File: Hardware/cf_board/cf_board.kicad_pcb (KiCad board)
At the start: 2 copper layers, 80.8 x 60.1 mm, 19 parts, among them J1 Conn_01x40, J2 Conn_02x25_Top_Bottom, U1 74HC00, U2 74HC00

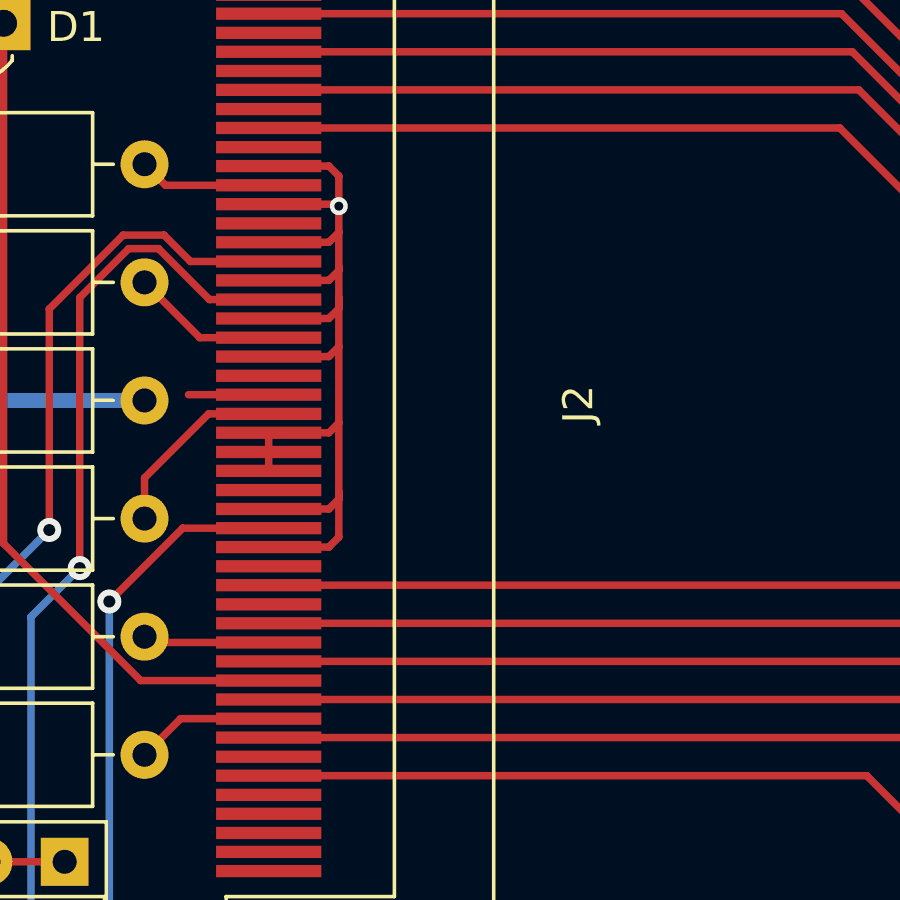
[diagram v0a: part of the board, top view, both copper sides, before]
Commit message: add jlc reference
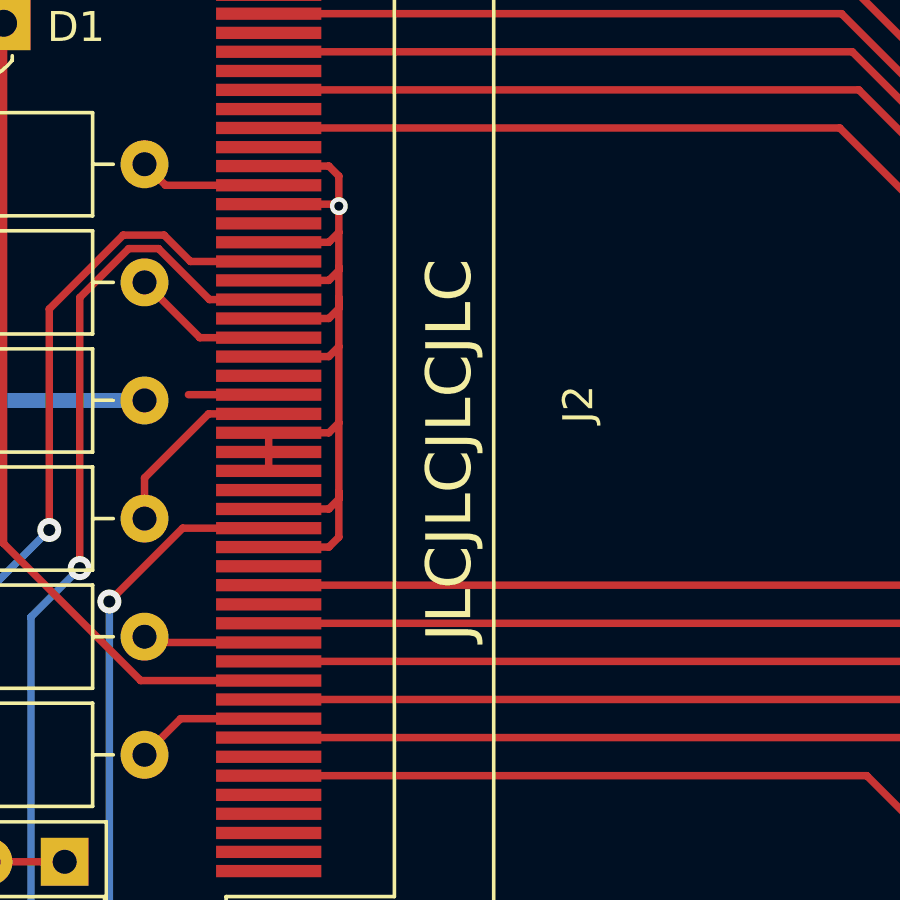
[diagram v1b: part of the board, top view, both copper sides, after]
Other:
- board text added: "JLCJLCJLCJLC"
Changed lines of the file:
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@@
     (effects (font (size 0.8 0.8) (thickness 0.15)))
+  )
+  (gr_text "JLCJLCJLCJLC" (at 120.65 86.614 90) (layer "F.SilkS")
+    (effects (font (size 1.5 1.5) (thickness 0.3)))
   )
   (gr_text "Compact Flash Board ${VERSION}" (at 81.407 68.707) (layer "F.SilkS")

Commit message: update with lcsc CF card socket
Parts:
- removed J2: Conn_02x25_Top_Bottom, Connector_Card:CF-Card_3M_N7E50-A516xx-30
- added J3: Conn_02x26_Top_Bottom, Custom_Footprints:SD-SMD_CFH-L3C1LBL01MN0, F.Cu at (121.7, 85.6)
- moved R2 19.7 mm to (110.5, 96.8)
- moved R3 19.7 mm to (110.5, 77.1)
- moved R1 11.8 mm to (110.5, 81.0)
- moved R4 11.8 mm to (110.5, 92.8)
- moved R5 3.94 mm to (110.5, 85.0)
- moved R6 3.94 mm to (97.8, 88.9)
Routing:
- net D3: track 69.6 -> 40.4 mm, vias 1 -> 0
- net D4: track 67.3 -> 38.9 mm
- net D5: track 65.2 -> 39.2 mm
- net D6: track 63.0 -> 38.5 mm
- net D7: track 60.3 -> 37.3 mm
- net D2: track 45.9 -> 68.3 mm, vias 0 -> 1
- net D1: track 49.0 -> 70.4 mm, vias 0 -> 1
- net D0: track 52.1 -> 72.5 mm, vias 0 -> 1
- net A0: track 50.6 -> 69.5 mm, vias 0 -> 1
- net A1: track 51.0 -> 65.8 mm
- net Net-(D1-Pad1): track 28.1 -> 14.9 mm
- net ~{RESET}: track 40.2 -> 49.6 mm
- net Net-(U2-Pad8): track 46.1 -> 36.9 mm
- net A2: track 51.8 -> 60.6 mm
- net Net-(U2-Pad11): track 39.1 -> 30.9 mm
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
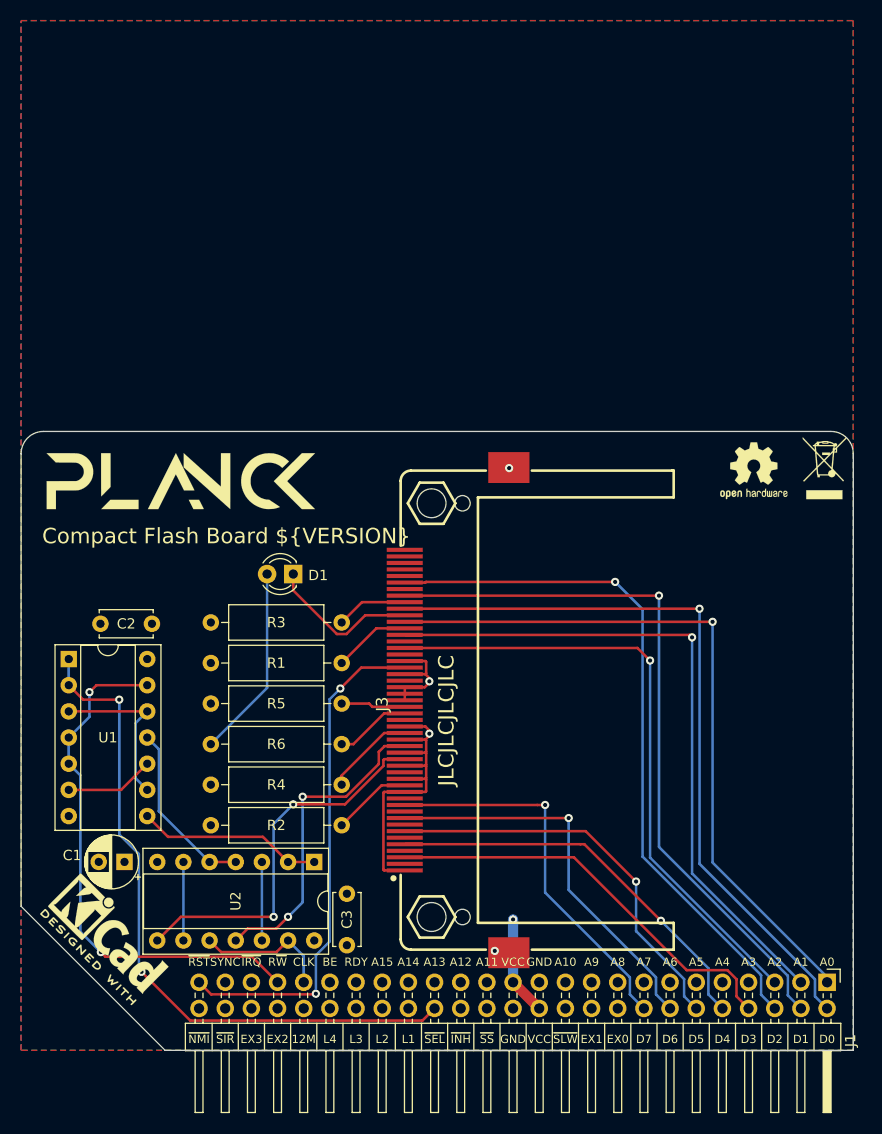
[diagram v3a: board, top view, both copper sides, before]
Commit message: CF card works as block storage for forth
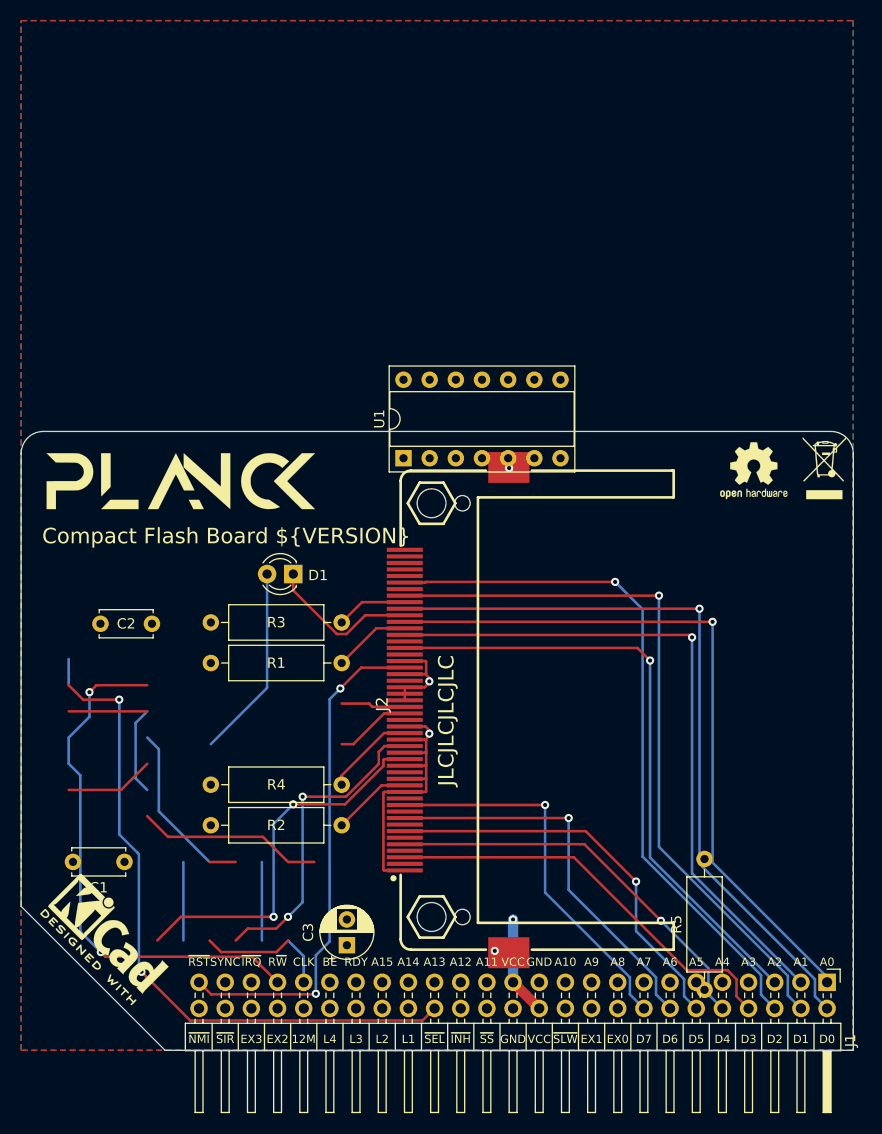
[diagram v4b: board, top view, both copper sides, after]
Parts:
- removed J3: Conn_02x26_Top_Bottom, Custom_Footprints:SD-SMD_CFH-L3C1LBL01MN0
- removed R6: 500R, Resistor_THT:R_Axial_DIN0309_L9.0mm_D3.2mm_P12.70mm_Horizontal
- removed U2: 74HC00, Package_DIP:DIP-14_W7.62mm_Socket
- added J2: Conn_02x26_Top_Bottom, Custom_Footprints:SD-SMD_CFH-L3C1LBL01MN0, F.Cu at (121.7, 85.6)
- C1: value 10u -> 100n; footprint Capacitor_THT:CP_Radial_D5.0mm_P2.50mm -> Capacitor_THT:C_Disc_D5.0mm_W2.5mm_P5.00mm
- C3: value 100n -> 10u; footprint Capacitor_THT:C_Disc_D5.0mm_W2.5mm_P5.00mm -> Capacitor_THT:CP_Radial_D5.0mm_P2.50mm
- R5: value 1k -> 500R
- moved R5 44.9 mm to (145.7, 112.7), turned to 90 degrees
- moved U1 37.9 mm to (116.5, 61.1), turned to 90 degrees
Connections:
- R5 pad 1: Net-(R5-Pad1) -> Net-(D1-Pad2)
- U1 pad 1: ~{SLOT_SEL} -> (no net)
- U1 pad 10: Net-(U1-Pad10) -> CLK
- U1 pad 13: R~{W} -> CLK
- U1 pad 2: ~{SLOT_SEL} -> (no net)
- U1 pad 3: Net-(U1-Pad12) -> (no net)
- U1 pad 6: Net-(U1-Pad10) -> Net-(U1-Pad12)
- U1 pad 9: Net-(U1-Pad12) -> R~{W}
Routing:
- net (no net): track 0.00 -> 58.1 mm
- net GND: track 40.8 -> 92.4 mm, vias 4 -> 5
- net Net-(U2-Pad8): track 36.9 -> 0.00 mm, vias 2 -> 0
- net R~{W}: track 51.6 -> 17.1 mm, vias 2 -> 1
- net Net-(U2-Pad11): track 30.9 -> 0.00 mm, vias 2 -> 0
- net Net-(J2-Pad34): track 18.1 -> 36.9 mm, vias 0 -> 2
- net Net-(U1-Pad12): track 16.2 -> 0.00 mm
- net Net-(J2-Pad35): track 17.1 -> 30.9 mm, vias 0 -> 2
- net Net-(U1-Pad10): track 8.67 -> 0.00 mm
- net Net-(U2-Pad6): track 7.62 -> 0.00 mm
- net Net-(U2-Pad12): track 7.62 -> 0.00 mm
- net +5V: track 17.1 -> 23.3 mm
- net Net-(R5-Pad1): track 6.26 -> 0.00 mm

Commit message: Add clock stretching + Simplify decoding.
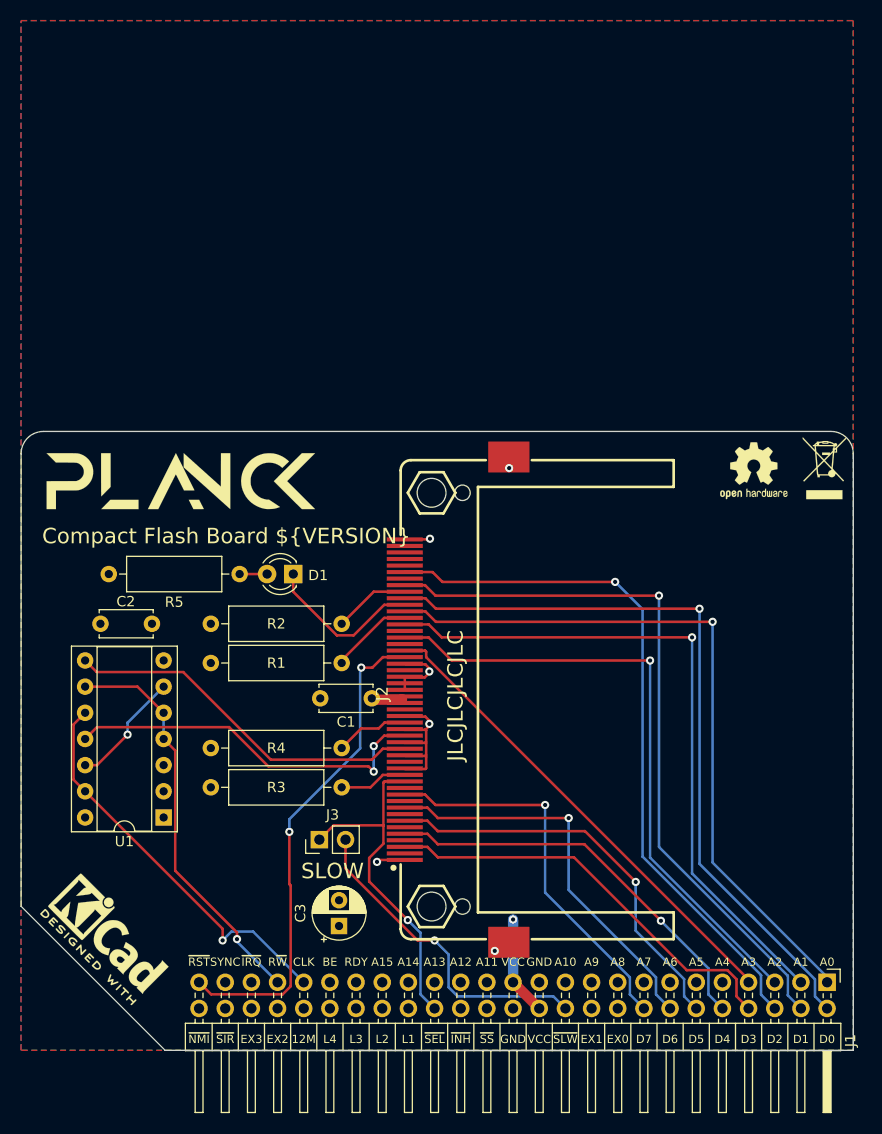
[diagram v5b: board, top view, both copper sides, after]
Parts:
- added J3: Conn_01x02, Connector_PinHeader_2.54mm:PinHeader_1x02_P2.54mm_Vertical, F.Cu at (108.3, 98.2)
- moved R5 60.5 mm to (100.6, 72.4), turned to 180 degrees
- moved U1 41.9 mm to (93.2, 96.0), turned to 180 degrees
- moved C1 28.8 mm to (113.4, 84.5)
- moved R2 19.6 mm to (110.5, 77.2)
- moved R3 16.0 mm to (110.5, 93.1)
- moved R4 3.56 mm to (110.5, 89.3)
- moved C3 2.01 mm to (110.2, 106.6)
- moved J2 1.02 mm to (121.7, 84.6)
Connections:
- J2 pad 17: GND -> A3
- U1 pad 1: (no net) -> GND
- U1 pad 2: (no net) -> GND
- U1 pad 3: (no net) -> unconnected-(U1-Pad3)
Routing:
- net GND: track 92.4 -> 27.6 mm, vias 5 -> 6
- net (no net): track 58.1 -> 0.00 mm
- net A3: track 0.00 -> 47.2 mm
- net ~{SLOT_SEL}: track 66.2 -> 34.0 mm, vias 2 -> 1
- net ~{SLOW}: track 0.00 -> 31.6 mm, vias 0 -> 1
- net CLK: track 13.2 -> 38.8 mm, vias 0 -> 1
- net R~{W}: track 17.1 -> 39.4 mm
- net Net-(D1-Pad2): track 18.8 -> 2.67 mm
- net Net-(U1-Pad12): track 0.00 -> 11.5 mm, vias 0 -> 1
- net +5V: track 23.3 -> 12.7 mm
- net Net-(J2-Pad35): track 30.9 -> 36.2 mm
- net Net-(J2-Pad36): track 8.73 -> 7.15 mm
- net Net-(J2-Pad34): track 36.9 -> 35.5 mm, vias 2 -> 0
- net ~{RESET}: track 49.6 -> 48.2 mm
- net Net-(D1-Pad1): track 14.9 -> 15.5 mm
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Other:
- board text added: "SLOW"

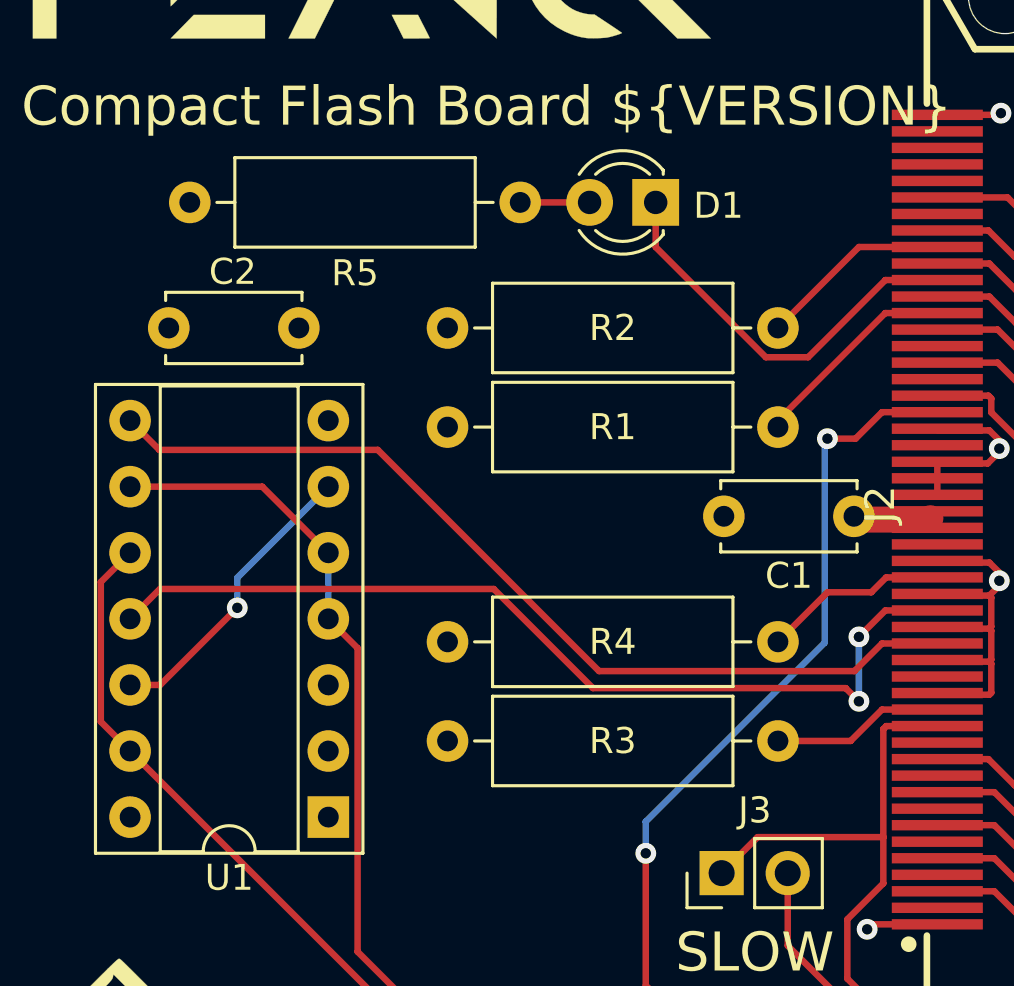
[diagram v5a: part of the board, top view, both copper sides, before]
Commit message: Smaller resistors for CF card.
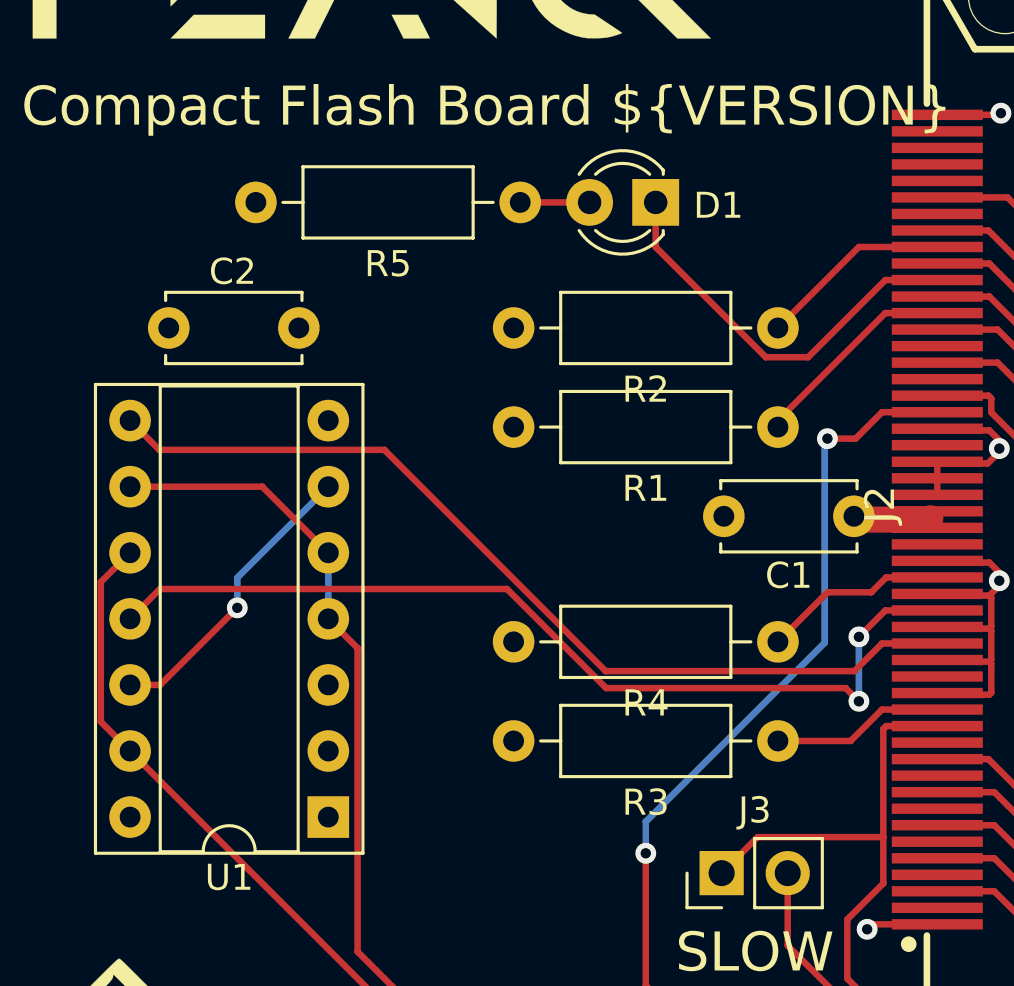
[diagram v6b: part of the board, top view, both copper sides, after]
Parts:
- R1, R2, R3, R4, R5: footprint Resistor_THT:R_Axial_DIN0309_L9.0mm_D3.2mm_P12.70mm_Horizontal -> Resistor_THT:R_Axial_DIN0207_L6.3mm_D2.5mm_P10.16mm_Horizontal
